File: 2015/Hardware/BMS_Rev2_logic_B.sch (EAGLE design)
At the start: 35 parts, among them Q9 MOSFET-NCHANNEL2N7002PW

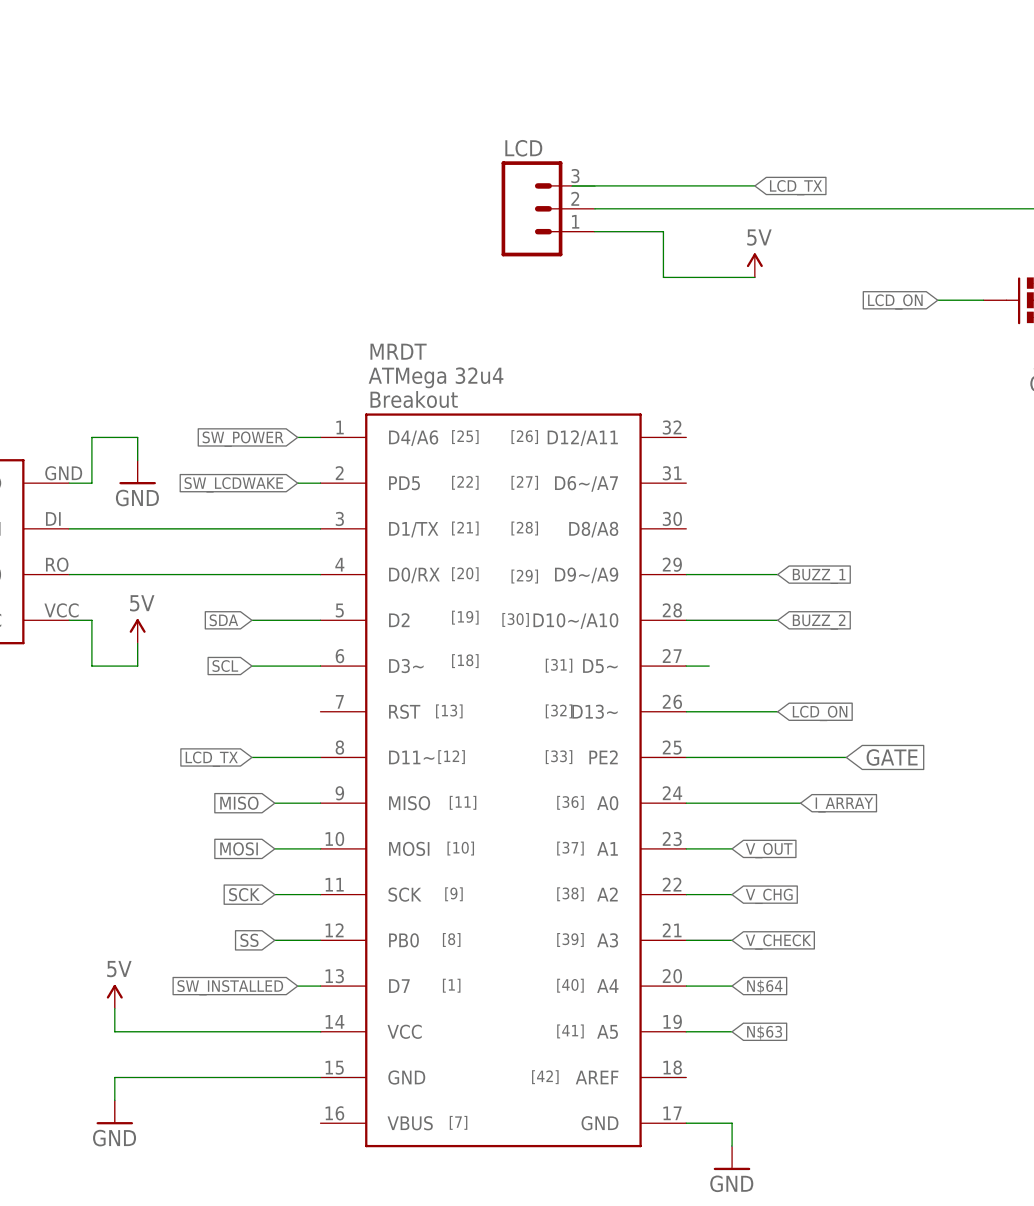
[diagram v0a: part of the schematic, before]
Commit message: Pinswapped on the schematic side to make traces easier.
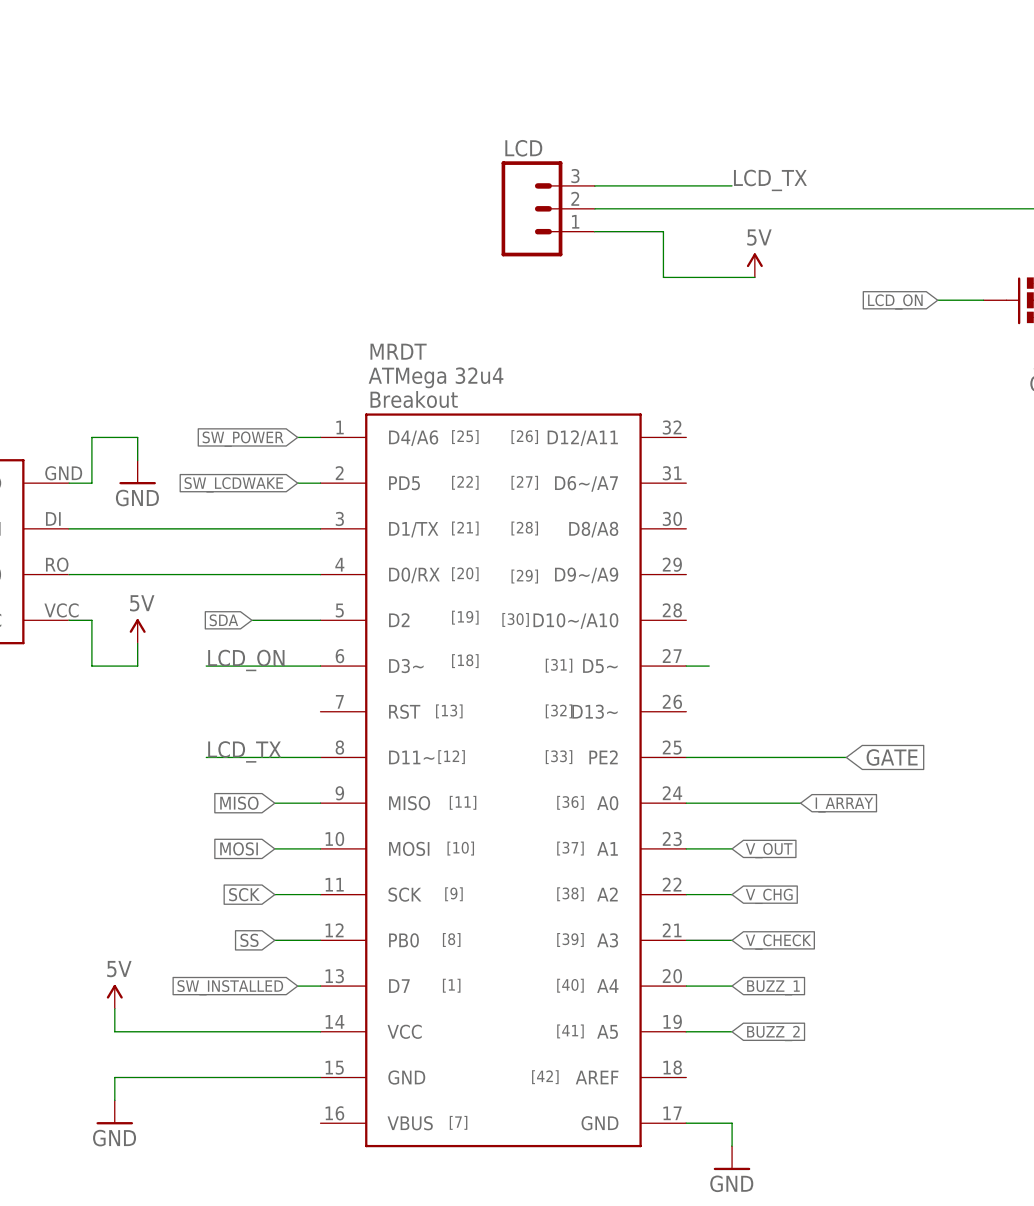
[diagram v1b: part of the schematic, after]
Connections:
- removed net N$63: U$3.A5
- removed net N$64: U$3.A4
- removed net SCL: U$3.D3~
- net BUZZ_1: now also U$3.A4; no longer U$3.D9~/A9
- net BUZZ_2: now also U$3.A5; no longer U$3.D10~/A10
- net LCD_ON: now also U$3.D3~; no longer U$3.D13~
- net LCD_TX: now also LCD.3
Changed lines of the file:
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@@
-</segment>
-</net>
-<net name="SCL" class="0">
-<segment>
-<pinref part="U$3" gate="G$1" pin="D3~"/>
-<wire x1="-53.34" y1="-35.56" x2="-60.96" y2="-35.56" width="0.1524" layer="91"/>
-<label x="-60.96" y="-35.56" size="1.27" layer="95" rot="R180" xref="yes"/>
 </segment>
 </net>
@@
 </segment>
 <segment>
-<pinref part="U$3" gate="G$1" pin="D13~"/>
-<wire x1="-12.7" y1="-40.64" x2="-2.54" y2="-40.64" width="0.1524" layer="91"/>
-<label x="-2.54" y="-40.64" size="1.27" layer="95" xref="yes"/>
+<pinref part="U$3" gate="G$1" pin="D3~"/>
+<wire x1="-53.34" y1="-35.56" x2="-66.04" y2="-35.56" width="0.1524" layer="91"/>
+<label x="-66.04" y="-35.56" size="1.778" layer="95"/>
 </segment>
 </net>
@@
 </segment>
 <segment>
-<pinref part="U$3" gate="G$1" pin="D9~/A9"/>
-<wire x1="-12.7" y1="-25.4" x2="-2.54" y2="-25.4" width="0.1524" layer="91"/>
-<label x="-2.54" y="-25.4" size="1.27" layer="95" xref="yes"/>
+<pinref part="U$3" gate="G$1" pin="A4"/>
+<wire x1="-12.7" y1="-71.12" x2="-7.62" y2="-71.12" width="0.1524" layer="91"/>
+<label x="-7.62" y="-71.12" size="1.27" layer="95" xref="yes"/>
 </segment>
 </net>
@@
 </segment>
 <segment>
-<pinref part="U$3" gate="G$1" pin="D10~/A10"/>
-<wire x1="-12.7" y1="-30.48" x2="-2.54" y2="-30.48" width="0.1524" layer="91"/>
-<label x="-2.54" y="-30.48" size="1.27" layer="95" xref="yes"/>
-</segment>
-</net>
-<net name="N$63" class="0">
-<segment>
 <pinref part="U$3" gate="G$1" pin="A5"/>
 <wire x1="-12.7" y1="-76.2" x2="-7.62" y2="-76.2" width="0.1524" layer="91"/>
 <label x="-7.62" y="-76.2" size="1.27" layer="95" xref="yes"/>
-</segment>
-</net>
-<net name="N$64" class="0">
-<segment>
-<pinref part="U$3" gate="G$1" pin="A4"/>
-<wire x1="-12.7" y1="-71.12" x2="-7.62" y2="-71.12" width="0.1524" layer="91"/>
-<label x="-7.62" y="-71.12" size="1.27" layer="95" xref="yes"/>
 </segment>
 </net>
@@
 </segment>
 </net>
-<net name="LCD_TX" class="0">
-<segment>
-<wire x1="-25.4" y1="17.78" x2="-5.08" y2="17.78" width="0.1524" layer="91"/>
-<label x="-5.08" y="17.78" size="1.27" layer="95" xref="yes"/>
-</segment>
-<segment>
-<pinref part="U$3" gate="G$1" pin="D11~"/>
-<wire x1="-53.34" y1="-45.72" x2="-60.96" y2="-45.72" width="0.1524" layer="91"/>
-<label x="-60.96" y="-45.72" size="1.27" layer="95" rot="R180" xref="yes"/>
-</segment>
-</net>
 <net name="N$5" class="0">
 <segment>
@@
 </segment>
 </net>
+<net name="LCD_TX" class="0">
+<segment>
+<pinref part="U$3" gate="G$1" pin="D11~"/>
+<wire x1="-53.34" y1="-45.72" x2="-66.04" y2="-45.72" width="0.1524" layer="91"/>
+<label x="-66.04" y="-45.72" size="1.778" layer="95"/>
+</segment>
+<segment>
+<pinref part="LCD" gate="G$1" pin="3"/>
+<wire x1="-22.86" y1="17.78" x2="-7.62" y2="17.78" width="0.1524" layer="91"/>
+<label x="-7.62" y="17.78" size="1.778" layer="95"/>
+</segment>
+</net>

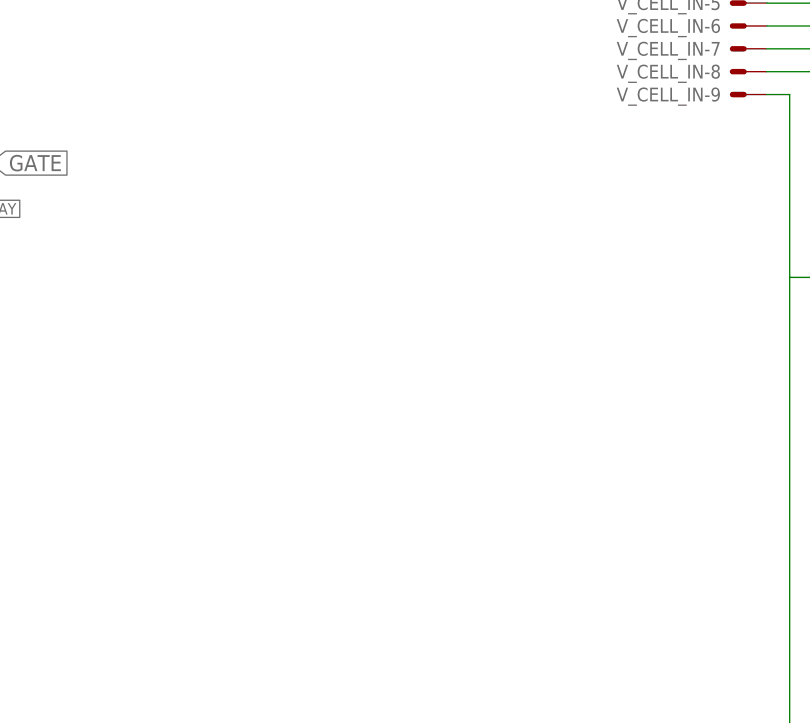
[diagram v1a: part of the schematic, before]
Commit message: Added Mounting Holes
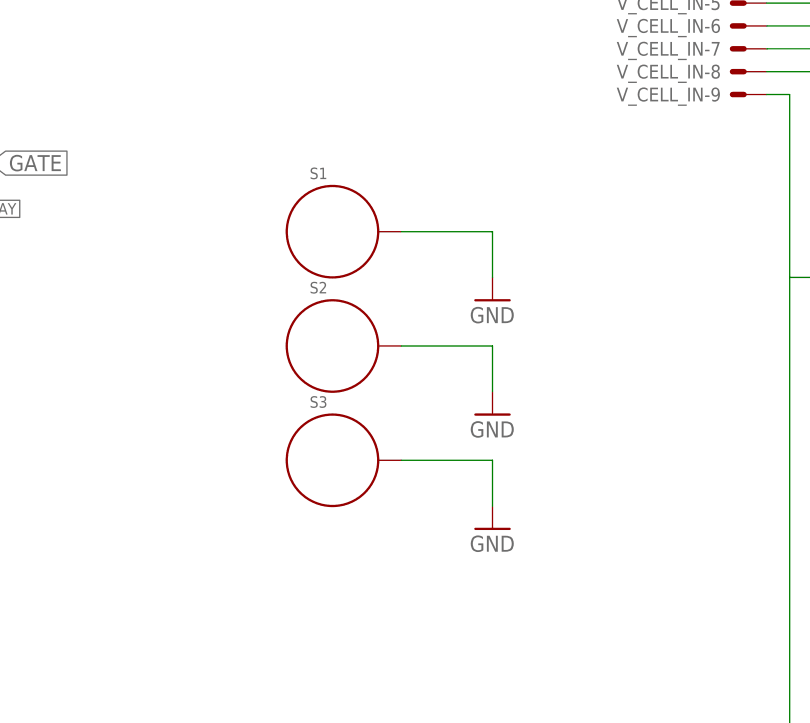
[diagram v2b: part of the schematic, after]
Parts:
- added S1, S2, S3: STANDOFF_ELECTRICAL, SparkFun-Electromechanical:STANDOFF_ELECTRICAL
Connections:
- net GND: now also S1.P$1, S2.P$1, S3.P$1
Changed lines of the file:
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@@
 <part name="LCD" library="SparkFun-Connectors" deviceset="M03" device="POLAR"/>
 <part name="SUPPLY3" library="SparkFun-Aesthetics" deviceset="5V" device=""/>
+<part name="S1" library="SparkFun-Electromechanical" deviceset="STANDOFF_ELECTRICAL" device=""/>
+<part name="S2" library="SparkFun-Electromechanical" deviceset="STANDOFF_ELECTRICAL" device=""/>
+<part name="S3" library="SparkFun-Electromechanical" deviceset="STANDOFF_ELECTRICAL" device=""/>
+<part name="GND3" library="SparkFun-Aesthetics" deviceset="GND" device=""/>
+<part name="GND4" library="SparkFun-Aesthetics" deviceset="GND" device=""/>
+<part name="GND5" library="SparkFun-Aesthetics" deviceset="GND" device=""/>
 </parts>
 <sheets>
@@
 <instance part="LCD" gate="G$1" x="-30.48" y="15.24"/>
 <instance part="SUPPLY3" gate="G$1" x="-5.08" y="7.62"/>
+<instance part="S1" gate="G$1" x="43.18" y="-53.34"/>
+<instance part="S2" gate="G$1" x="43.18" y="-66.04"/>
+<instance part="S3" gate="G$1" x="43.18" y="-78.74"/>
+<instance part="GND3" gate="1" x="60.96" y="-60.96"/>
+<instance part="GND4" gate="1" x="60.96" y="-73.66"/>
+<instance part="GND5" gate="1" x="60.96" y="-86.36"/>
 </instances>
 <busses>
@@
 <pinref part="GND2" gate="1" pin="GND"/>
 </segment>
+<segment>
+<pinref part="S1" gate="G$1" pin="P$1"/>
+<wire x1="50.8" y1="-53.34" x2="60.96" y2="-53.34" width="0.1524" layer="91"/>
+<wire x1="60.96" y1="-53.34" x2="60.96" y2="-58.42" width="0.1524" layer="91"/>
+<pinref part="GND3" gate="1" pin="GND"/>
+</segment>
+<segment>
+<pinref part="S2" gate="G$1" pin="P$1"/>
+<wire x1="50.8" y1="-66.04" x2="60.96" y2="-66.04" width="0.1524" layer="91"/>
+<wire x1="60.96" y1="-66.04" x2="60.96" y2="-71.12" width="0.1524" layer="91"/>
+<pinref part="GND4" gate="1" pin="GND"/>
+</segment>
+<segment>
+<pinref part="S3" gate="G$1" pin="P$1"/>
+<wire x1="50.8" y1="-78.74" x2="60.96" y2="-78.74" width="0.1524" layer="91"/>
+<wire x1="60.96" y1="-78.74" x2="60.96" y2="-83.82" width="0.1524" layer="91"/>
+<pinref part="GND5" gate="1" pin="GND"/>
+</segment>
 </net>

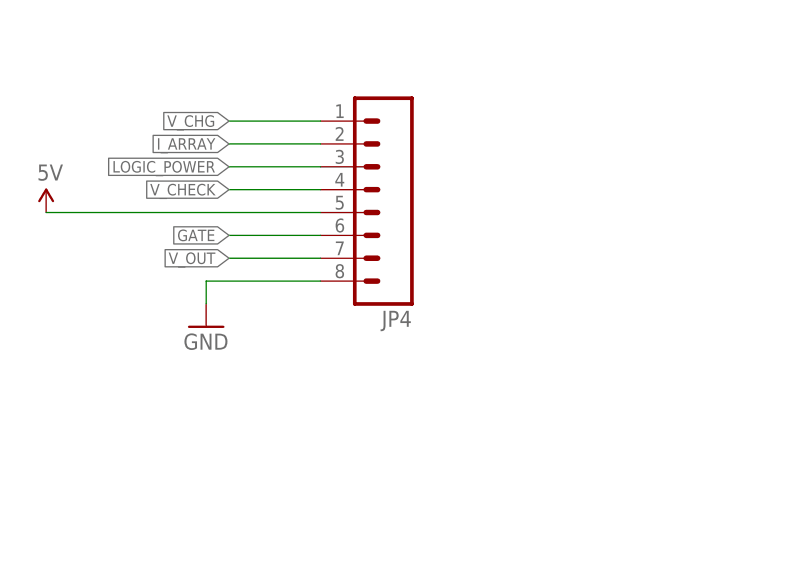
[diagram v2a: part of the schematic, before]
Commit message: Changed the connector. The connector from the SSR to the logic board to a more standard connector.
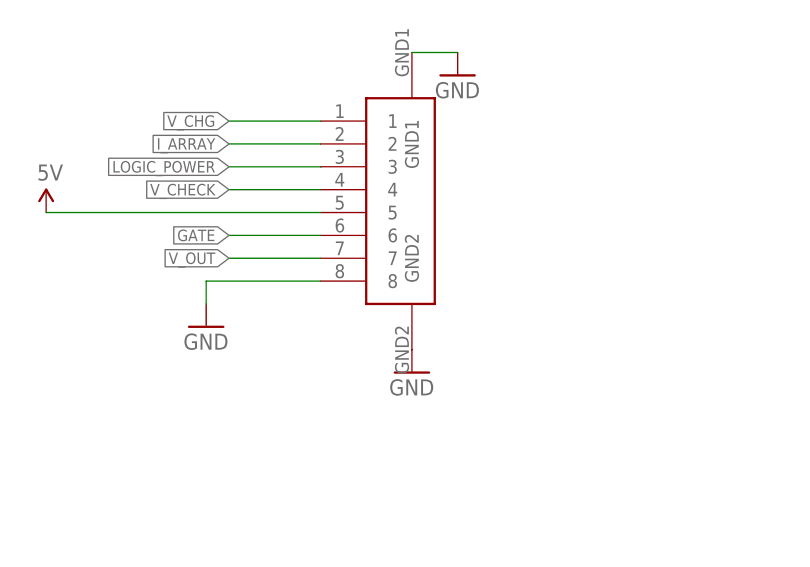
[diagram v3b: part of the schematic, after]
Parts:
- removed JP4: (no value), SparkFun-Connectors:M08BM08B-SRSS-TB
- added U$1: 8POS_LOGIC, New:8POS_LOGIC
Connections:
- net 5V: now also U$1.5; no longer JP4.5
- net GATE: now also U$1.6; no longer JP4.6
- net GND: now also U$1.8, U$1.GND1, U$1.GND2; no longer JP4.8
- net I_ARRAY: now also U$1.2; no longer JP4.2
- net LOGIC_POWER: now also U$1.3; no longer JP4.3
- net V_CHECK: now also U$1.4; no longer JP4.4
- net V_CHG: now also U$1.1; no longer JP4.1
- net V_OUT: now also U$1.7; no longer JP4.7
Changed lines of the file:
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@@
 <part name="F7" library="SparkFun-PowerIC" deviceset="PTC" device="SMD"/>
 <part name="F8" library="SparkFun-PowerIC" deviceset="PTC" device="SMD"/>
-<part name="JP4" library="SparkFun-Connectors" deviceset="M08" device="BM08B-SRSS-TB"/>
 <part name="SUPPLY2" library="SparkFun-Aesthetics" deviceset="5V" device=""/>
 <part name="GND2" library="SparkFun-Aesthetics" deviceset="GND" device=""/>
@@
 <part name="GND4" library="SparkFun-Aesthetics" deviceset="GND" device=""/>
 <part name="GND5" library="SparkFun-Aesthetics" deviceset="GND" device=""/>
+<part name="U$1" library="New" deviceset="8POS_LOGIC" device=""/>
+<part name="GND6" library="SparkFun-Aesthetics" deviceset="GND" device=""/>
+<part name="GND7" library="SparkFun-Aesthetics" deviceset="GND" device=""/>
 </parts>
 <sheets>
@@
 <instance part="F7" gate="G$1" x="134.62" y="-48.26"/>
 <instance part="F8" gate="G$1" x="121.92" y="-53.34"/>
-<instance part="JP4" gate="G$1" x="-10.16" y="99.06" rot="R180"/>
 <instance part="SUPPLY2" gate="G$1" x="-45.72" y="96.52"/>
 <instance part="GND2" gate="1" x="-27.94" y="83.82"/>
@@
 <instance part="GND4" gate="1" x="60.96" y="-73.66"/>
 <instance part="GND5" gate="1" x="60.96" y="-86.36"/>
+<instance part="U$1" gate="G$1" x="-10.16" y="91.44"/>
+<instance part="GND6" gate="1" x="-5.08" y="78.74"/>
+<instance part="GND7" gate="1" x="0" y="111.76"/>
 </instances>
 <busses>
@@
 </segment>
 <segment>
-<pinref part="JP4" gate="G$1" pin="5"/>
 <wire x1="-15.24" y1="96.52" x2="-45.72" y2="96.52" width="0.1524" layer="91"/>
 <pinref part="SUPPLY2" gate="G$1" pin="5V"/>
+<pinref part="U$1" gate="G$1" pin="5"/>
 </segment>
 <segment>
@@
 </segment>
 <segment>
-<pinref part="JP4" gate="G$1" pin="8"/>
 <wire x1="-15.24" y1="88.9" x2="-27.94" y2="88.9" width="0.1524" layer="91"/>
 <wire x1="-27.94" y1="88.9" x2="-27.94" y2="86.36" width="0.1524" layer="91"/>
 <pinref part="GND2" gate="1" pin="GND"/>
+<pinref part="U$1" gate="G$1" pin="8"/>
 </segment>
 <segment>
@@
 <pinref part="GND5" gate="1" pin="GND"/>
 </segment>
+<segment>
+<pinref part="U$1" gate="G$1" pin="GND2"/>
+<pinref part="GND6" gate="1" pin="GND"/>
+</segment>
+<segment>
+<pinref part="U$1" gate="G$1" pin="GND1"/>
+<pinref part="GND7" gate="1" pin="GND"/>
+<wire x1="-5.08" y1="114.3" x2="0" y2="114.3" width="0.1524" layer="91"/>
+</segment>
 </net>
 <net name="GATE" class="0">
@@
 </segment>
 <segment>
-<pinref part="JP4" gate="G$1" pin="6"/>
 <wire x1="-15.24" y1="93.98" x2="-25.4" y2="93.98" width="0.1524" layer="91"/>
 <label x="-25.4" y="93.98" size="1.27" layer="95" rot="R180" xref="yes"/>
+<pinref part="U$1" gate="G$1" pin="6"/>
 </segment>
 </net>
@@
 </segment>
 <segment>
-<pinref part="JP4" gate="G$1" pin="2"/>
 <wire x1="-15.24" y1="104.14" x2="-25.4" y2="104.14" width="0.1524" layer="91"/>
 <label x="-25.4" y="104.14" size="1.27" layer="95" rot="R180" xref="yes"/>
+<pinref part="U$1" gate="G$1" pin="2"/>
 </segment>
 </net>
@@
 <net name="V_OUT" class="0">
 <segment>
-<pinref part="JP4" gate="G$1" pin="7"/>
 <wire x1="-15.24" y1="91.44" x2="-25.4" y2="91.44" width="0.1524" layer="91"/>
 <label x="-25.4" y="91.44" size="1.27" layer="95" rot="R180" xref="yes"/>
+<pinref part="U$1" gate="G$1" pin="7"/>
 </segment>
 <segment>
@@
 <net name="V_CHECK" class="0">
 <segment>
-<pinref part="JP4" gate="G$1" pin="4"/>
 <wire x1="-15.24" y1="99.06" x2="-25.4" y2="99.06" width="0.1524" layer="91"/>
 <label x="-25.4" y="99.06" size="1.27" layer="95" rot="R180" xref="yes"/>
+<pinref part="U$1" gate="G$1" pin="4"/>
 </segment>
 <segment>
@@
 <net name="V_CHG" class="0">
 <segment>
-<pinref part="JP4" gate="G$1" pin="1"/>
 <wire x1="-15.24" y1="106.68" x2="-25.4" y2="106.68" width="0.1524" layer="91"/>
 <label x="-25.4" y="106.68" size="1.27" layer="95" rot="R180" xref="yes"/>
+<pinref part="U$1" gate="G$1" pin="1"/>
 </segment>
 <segment>
@@
 <net name="LOGIC_POWER" class="0">
 <segment>
-<pinref part="JP4" gate="G$1" pin="3"/>
 <wire x1="-15.24" y1="101.6" x2="-25.4" y2="101.6" width="0.1524" layer="91"/>
 <label x="-25.4" y="101.6" size="1.27" layer="95" rot="R180" xref="yes"/>
-</segment>
-<segment>
+<pinref part="U$1" gate="G$1" pin="3"/>
+</segment>
+<segment>

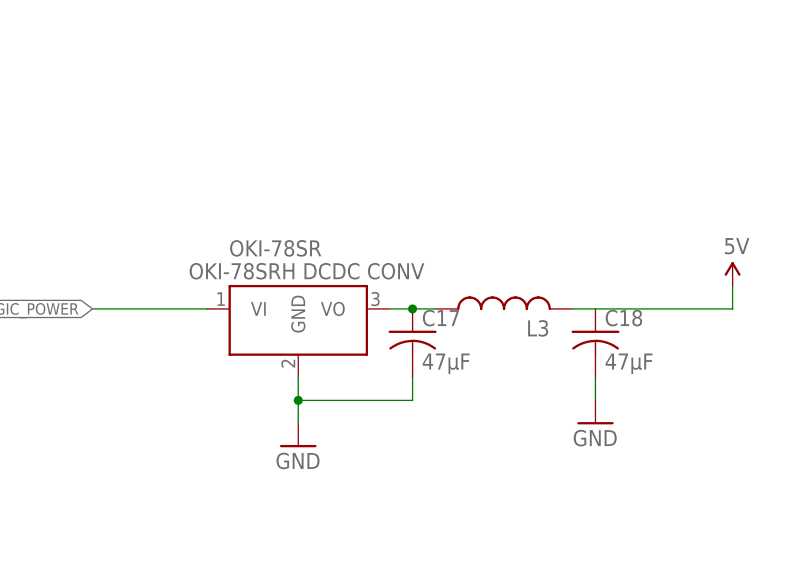
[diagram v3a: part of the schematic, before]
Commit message: New Inductor for the Pi Fitler
Pi Filter uses Fair-Rite 2773019447 as the inductor
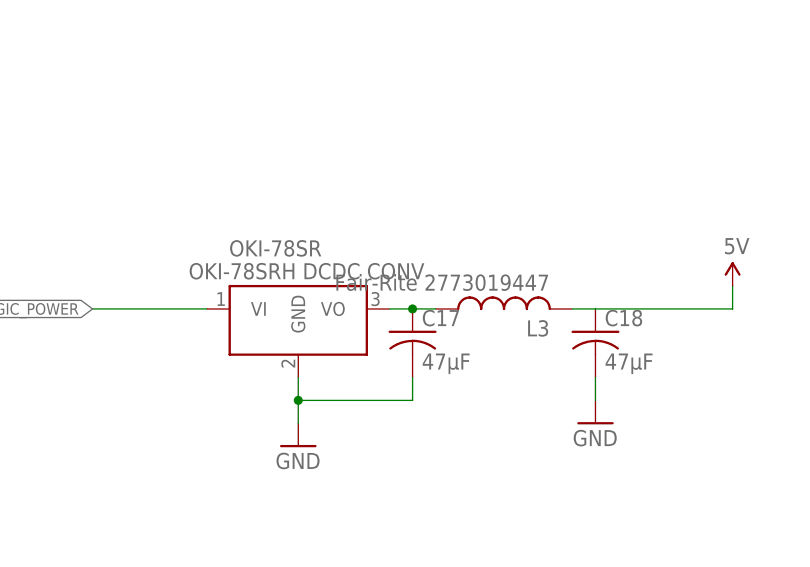
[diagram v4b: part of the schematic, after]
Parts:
- L3: value (none) -> Fair-Rite 2773019447; device resistor:L-USL3216C -> rcl:L-USL4532C
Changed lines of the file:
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@@
 <?xml version="1.0" encoding="utf-8"?>
 <!DOCTYPE eagle SYSTEM "eagle.dtd">
-<eagle version="6.5.0">
+<eagle version="7.0.0">
 <drawing>
 <settings>
@@
 <part name="GND1" library="SparkFun-Aesthetics" deviceset="GND" device=""/>
 <part name="C17" library="resistor" deviceset="C-US" device="C1206" value="47µF"/>
-<part name="L3" library="resistor" deviceset="L-US" device="L3216C"/>
+<part name="L3" library="rcl" deviceset="L-US" device="L4532C" value="Fair-Rite 2773019447"/>
 <part name="C18" library="resistor" deviceset="C-US" device="C1206" value="47µF"/>
 <part name="GND10" library="SparkFun-Aesthetics" deviceset="GND" device=""/>
